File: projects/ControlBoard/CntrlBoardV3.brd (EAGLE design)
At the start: 76.2 x 76.2 mm, 122 parts, among them J1 HARWIN_06, J2 HARWIN_06, J3 M80-54006, J4 M80-54010, J5 M80-54008, J6 M80-54020, J7 M83-LMT1M2N27, J8 M80-5101005, J9 M50-3600542, M1 AON7522E, M2 SI4427BDY-T1-E3CT-ND, U1 MR25H40MDF, U10 LT6015, U11 LT6016, U12 TPS63001, U13 TPS63002, U14 MPU9250, U15 HMC5883L, U2 M24M02-DR, U3 SN74LVC1G125, U4 SN74LVC1G125, U6 MR25H40MDF, U7 AD7991-1, U8 LTC1380-GN, U9 LTC1380-GN

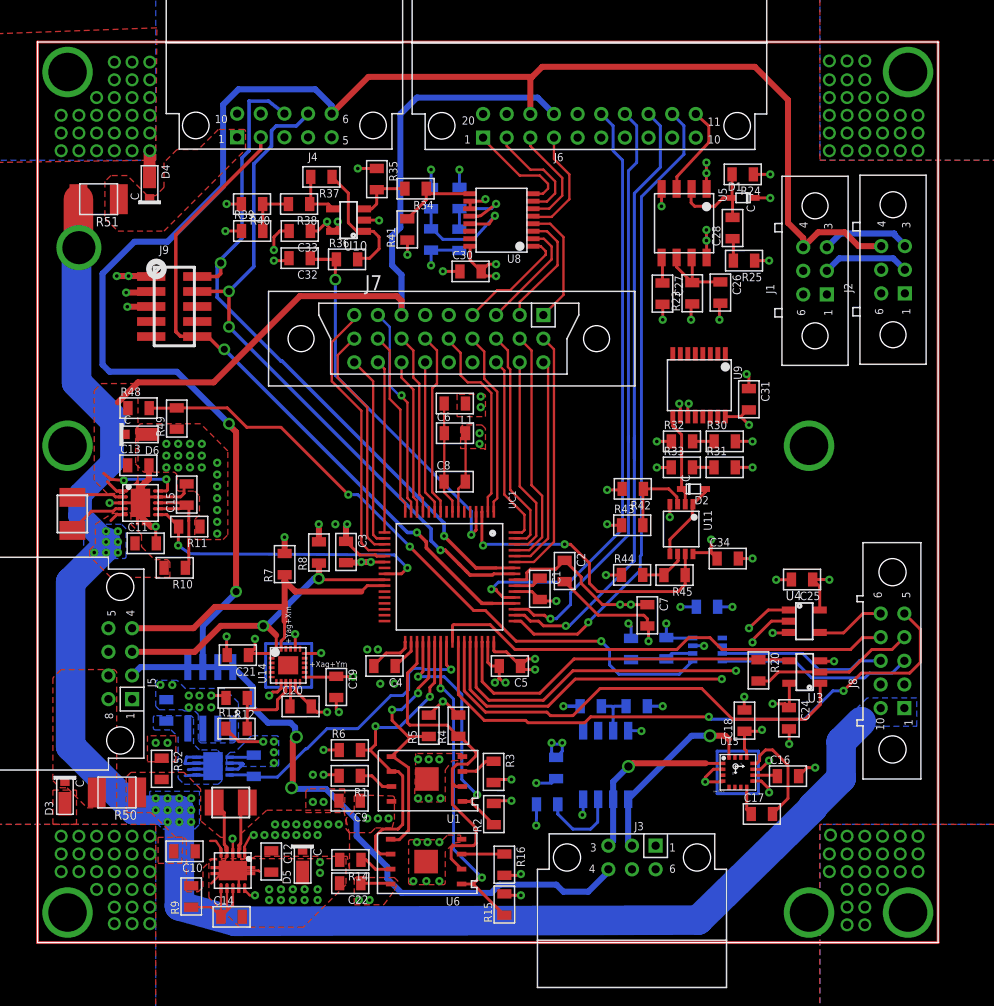
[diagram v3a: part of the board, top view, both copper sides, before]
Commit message: Completed first round of Control Board routing and silkscreen marker placement. Gonna sleep on it and see how I like it in the morning.
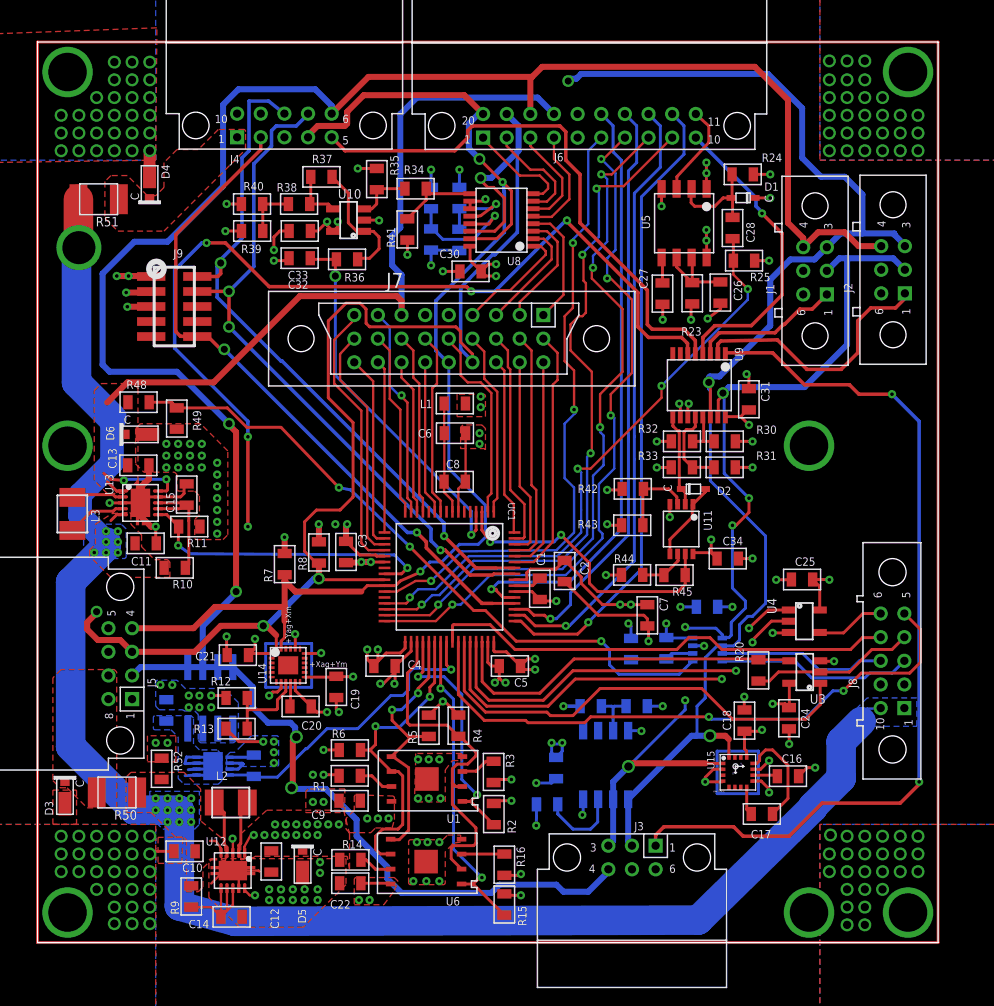
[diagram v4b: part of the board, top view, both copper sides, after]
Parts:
- moved R48 0.50 mm to (8.55, 45.7)
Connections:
- net PD_FLASH: now also U9.P$4; no longer U9.P$1
- net PD_XN: now also U9.P$2; no longer U9.P$3
- net PD_XP: now also U9.P$6; no longer U9.P$2
- net PD_YN: now also U9.P$3; no longer U9.P$4
- net PD_ZN: now also U9.P$5; no longer U9.P$6
- net PD_ZP: now also U9.P$1; no longer U9.P$5
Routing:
- net SDA: track 51.9 -> 331.7 mm, vias 3 -> 7
- net SCL: track 52.0 -> 264.9 mm, vias 1 -> 9
- net PD_XP: track 0.00 -> 99.4 mm, vias 0 -> 5
- net PD_ZP: track 0.00 -> 75.2 mm, vias 0 -> 2
- net ANT_DRV2: track 0.00 -> 60.0 mm, vias 0 -> 4
- net ANT_DRV1: track 0.00 -> 59.9 mm, vias 0 -> 4
- net ANT_DRV3: track 0.00 -> 59.7 mm, vias 0 -> 4
- net DET_RTN: track 0.00 -> 53.7 mm, vias 0 -> 3
- net !LED_CMD!: track 1.89 -> 51.8 mm, vias 0 -> 4
- net PD_ZN: track 0.00 -> 46.6 mm
- net PD_FLASH: track 0.00 -> 25.9 mm, vias 0 -> 1
- net PD_XN: track 0.00 -> 22.3 mm
- net N$32: track 15.2 -> 0.00 mm
- net N$31: track 15.2 -> 0.00 mm
- net N$30: track 14.2 -> 0.00 mm
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
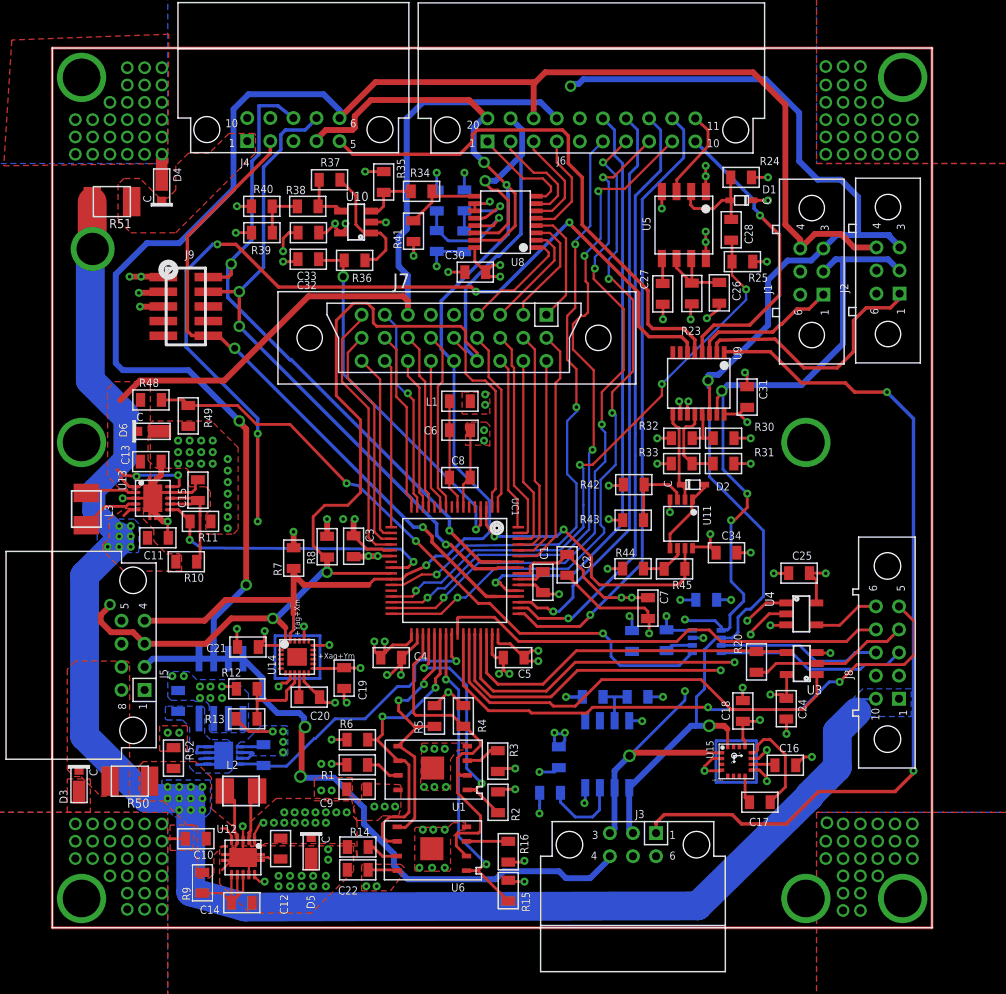
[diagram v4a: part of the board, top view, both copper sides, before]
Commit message: Added test vias and LEDs for testing and monitoring. Cleaned up asthetics and added documentation on silkscreen
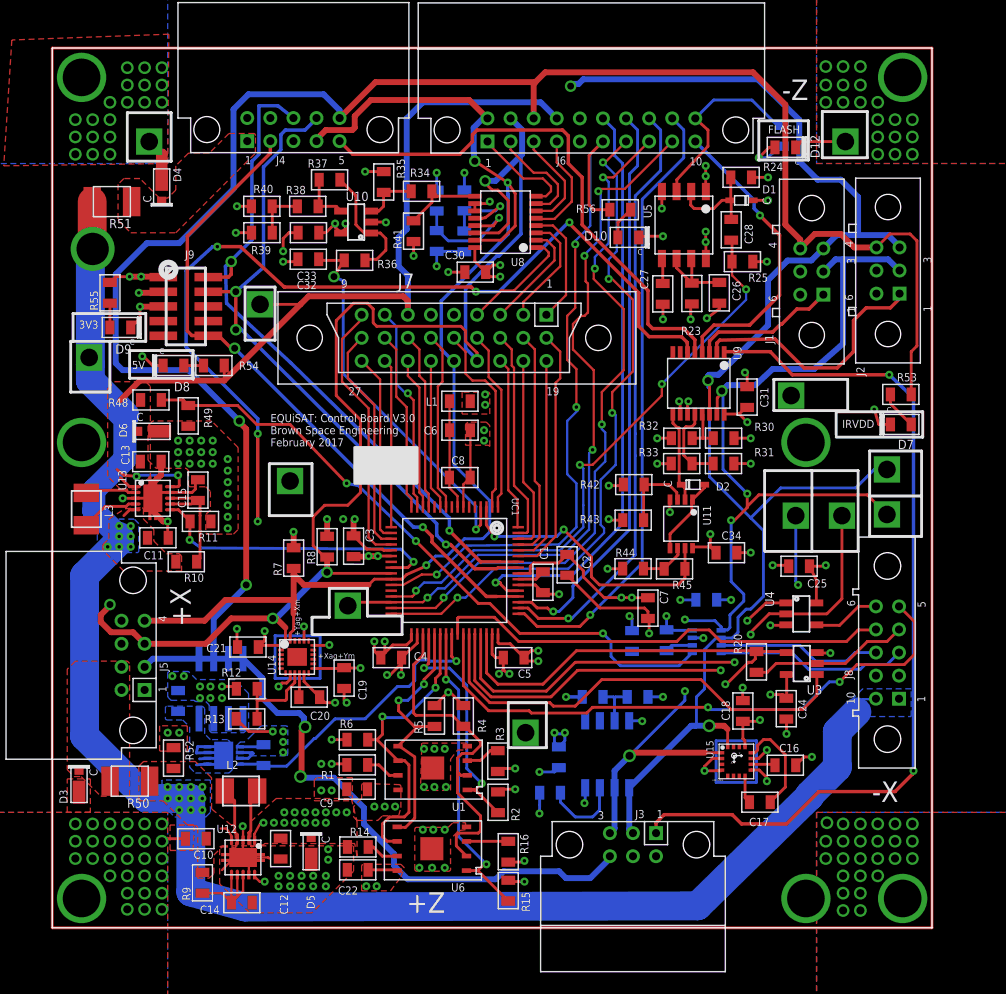
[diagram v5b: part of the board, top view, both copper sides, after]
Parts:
- added D10, D12, D7, D8, D9: LED0805, BrownSpaceEngineering:0805-D
- added R53, R55, R58: 330R, BrownSpaceEngineering:0805
- added R54, R56: 560R, BrownSpaceEngineering:0805
- added V1: RX_DATA, BrownSpaceEngineering:VIA-60MIL-SQ
- added V10, V11, V12, V9: GND, BrownSpaceEngineering:VIA-60MIL-SQ
- added V13: 3V3, BrownSpaceEngineering:VIA-60MIL-SQ
- added V14: 5V, BrownSpaceEngineering:VIA-60MIL-SQ
- added V2: TX_DATA, BrownSpaceEngineering:VIA-60MIL-SQ
- added V3: VIN, BrownSpaceEngineering:VIA-60MIL-SQ
- added V4: SDA, BrownSpaceEngineering:VIA-60MIL-SQ
- added V5: SCL, BrownSpaceEngineering:VIA-60MIL-SQ
- added V6: ANT_DRV1, BrownSpaceEngineering:VIA-60MIL-SQ
- moved C25 0.60 mm to (64.7, 31.3)
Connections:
- new net N$29: D7.A, R53.1
- new net N$30: D8.A, R54.1
- new net N$31: D9.A, R55.1
- new net N$40: D10.A, R56.1
- new net N$44: D12.A, R58.2
- net +3V3: now also R55.2, V13.P$1
- net +5V: now also R54.2, V14.P$1
- net ANT_DRV1: now also V6.P$1
- net DET_RTN: now also R56.2
- net GND: now also D10.C, D12.C, D7.C, D8.C, D9.C, V10.P$1, V11.P$1, V12.P$1, V9.P$1
- net IRVDD: now also R53.2
- net LED_SHDN: now also R58.1
- net RX_DATA: now also V1.P$1
- net SCL: now also V5.P$1
- net SDA: now also V4.P$1
- net TX_DATA: now also V2.P$1
- net VIN: now also V3.P$1
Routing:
- net RX_DATA: track 31.2 -> 52.6 mm, vias 0 -> 2
- net IRVDD: track 194.7 -> 212.4 mm
- net GND: track 144.8 -> 160.0 mm, vias 226 -> 211
- net SCL: track 264.9 -> 278.4 mm
- net SDA: track 331.7 -> 344.9 mm
- net TX_DATA: track 34.2 -> 46.8 mm
- net LED_SHDN: track 7.90 -> 17.0 mm
- net DET_RTN: track 53.7 -> 61.6 mm
- net +5V: track 70.4 -> 75.2 mm
- net N$44: track 0.00 -> 4.11 mm, vias 0 -> 1
- net ANT_DRV1: track 59.9 -> 63.7 mm
- net N$29: track 0.00 -> 3.35 mm
- net N$40: track 0.00 -> 2.86 mm
- net +3V3: track 123.0 -> 125.4 mm
- net N$31: track 0.00 -> 2.10 mm
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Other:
- board text added: "3V3"
- board text added: "5V"
- board text added: "EQUiSAT: Control Board V3.0 Brown Space Engineering February 2017"
- board text added: "FLASH"
- board text added: "IRVDD"

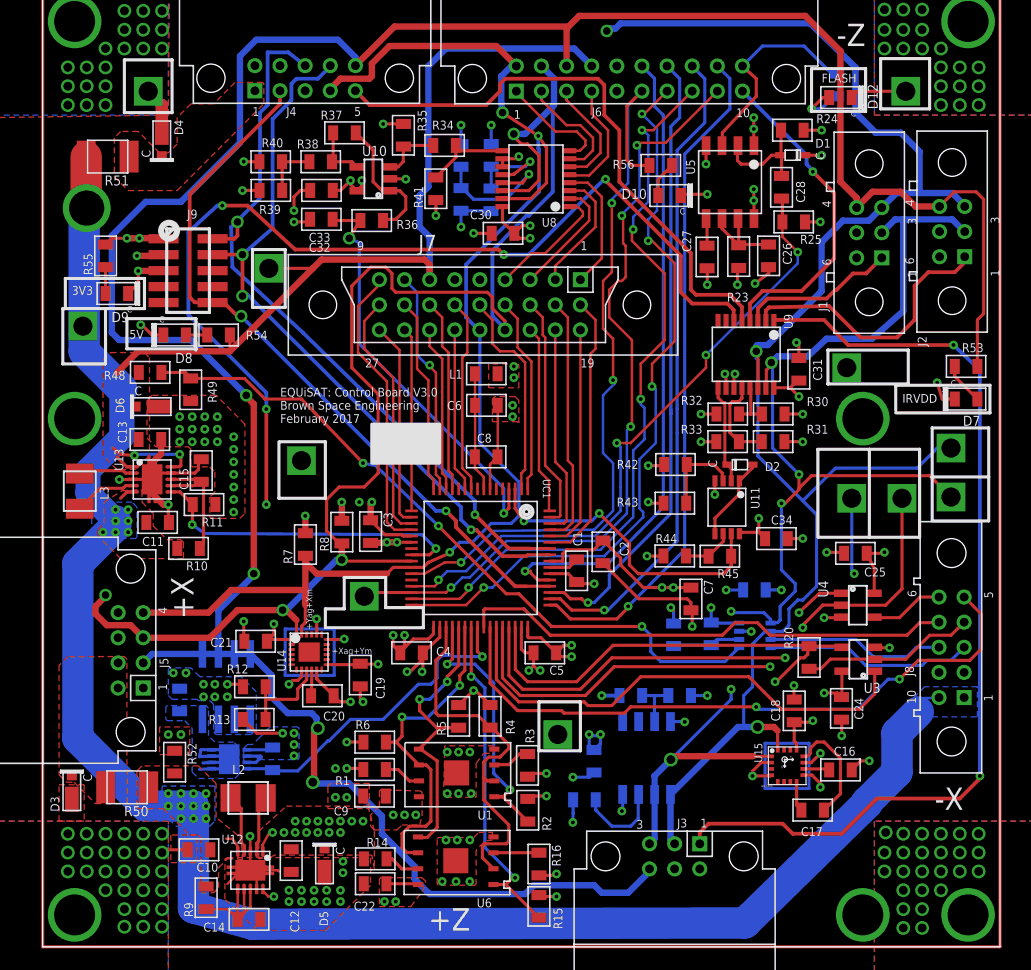
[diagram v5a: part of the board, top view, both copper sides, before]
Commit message: Cleaned up a few small things and corrected for errors discovered in DRC check.
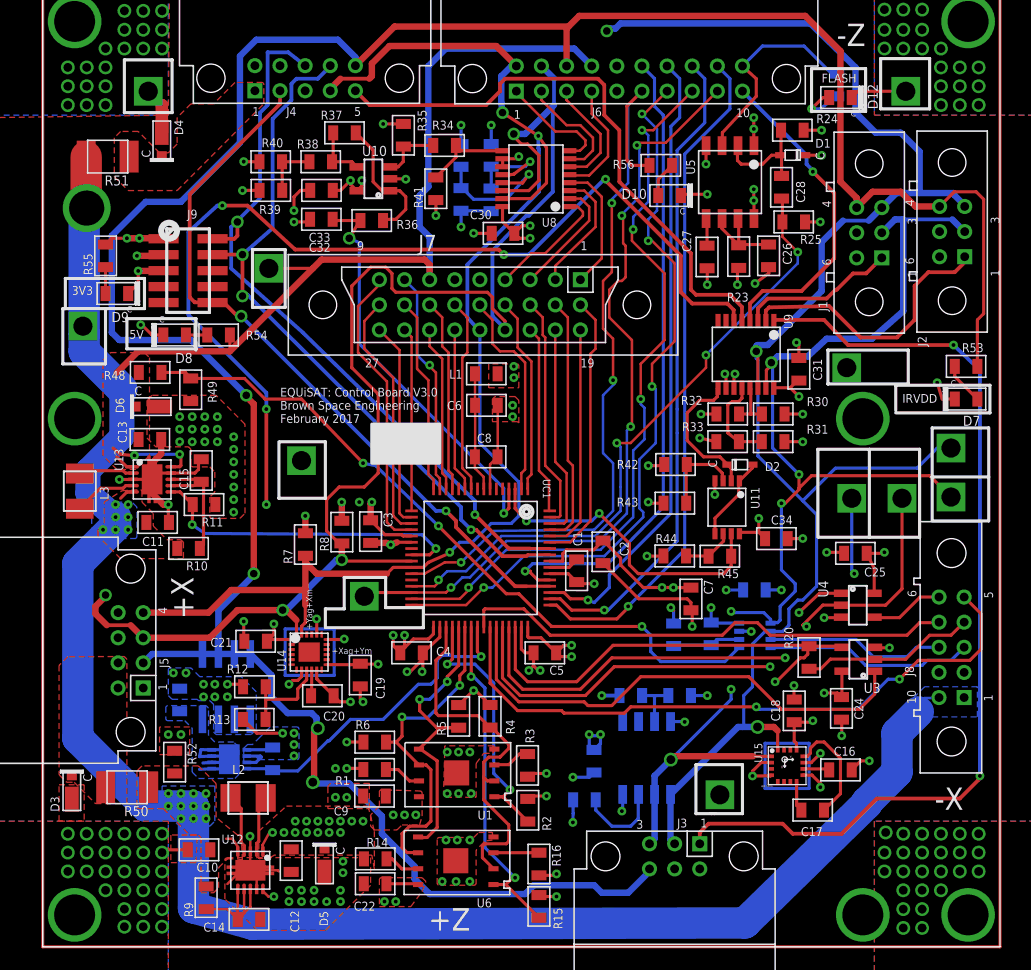
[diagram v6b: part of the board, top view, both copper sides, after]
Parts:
- moved V12 13.8 mm to (53.9, 12.1)
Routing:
- net PD_IN: track 7.92 -> 11.3 mm
- net GND: track 160.0 -> 160.1 mm, vias 211 -> 209
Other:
- board text removed: "Top layer is -Y side"

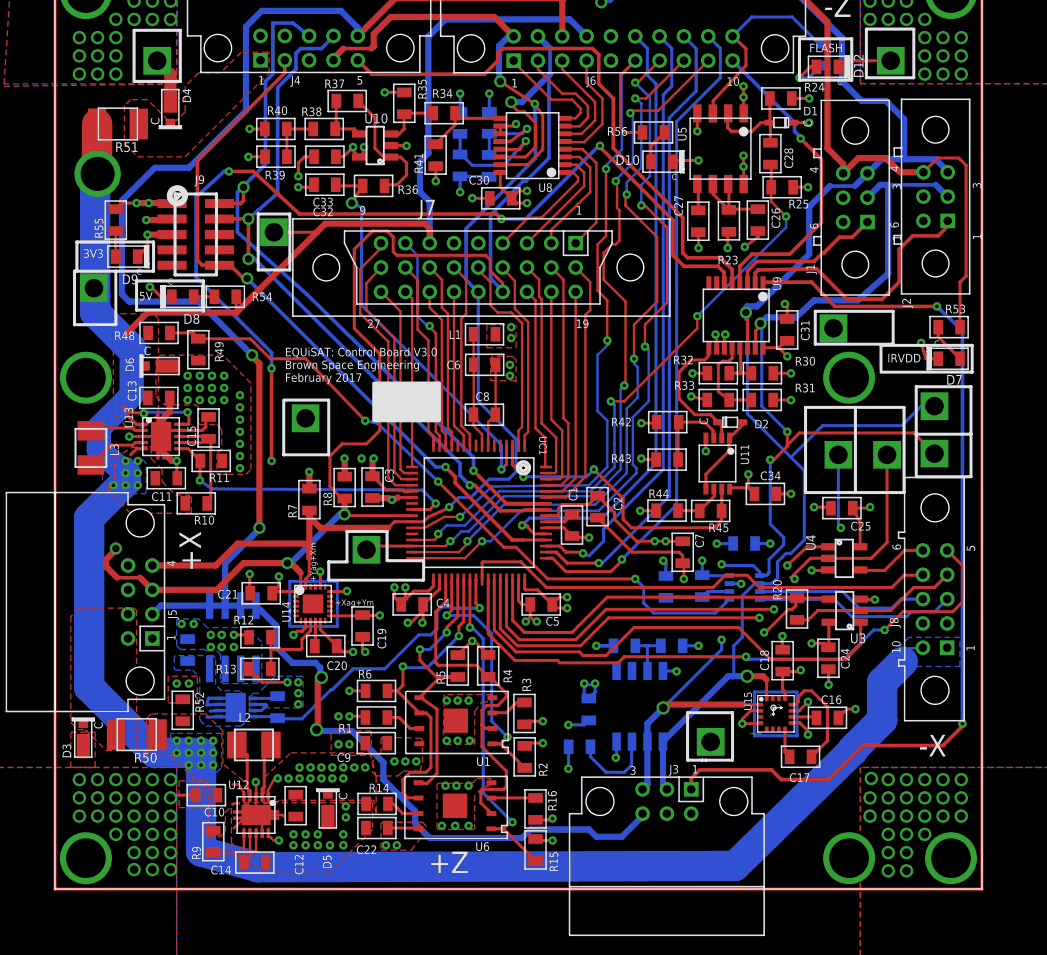
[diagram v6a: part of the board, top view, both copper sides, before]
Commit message: Fixed problem with processor pin mapping, rerouted accordingly. Final adjustments for production. Ready to order.
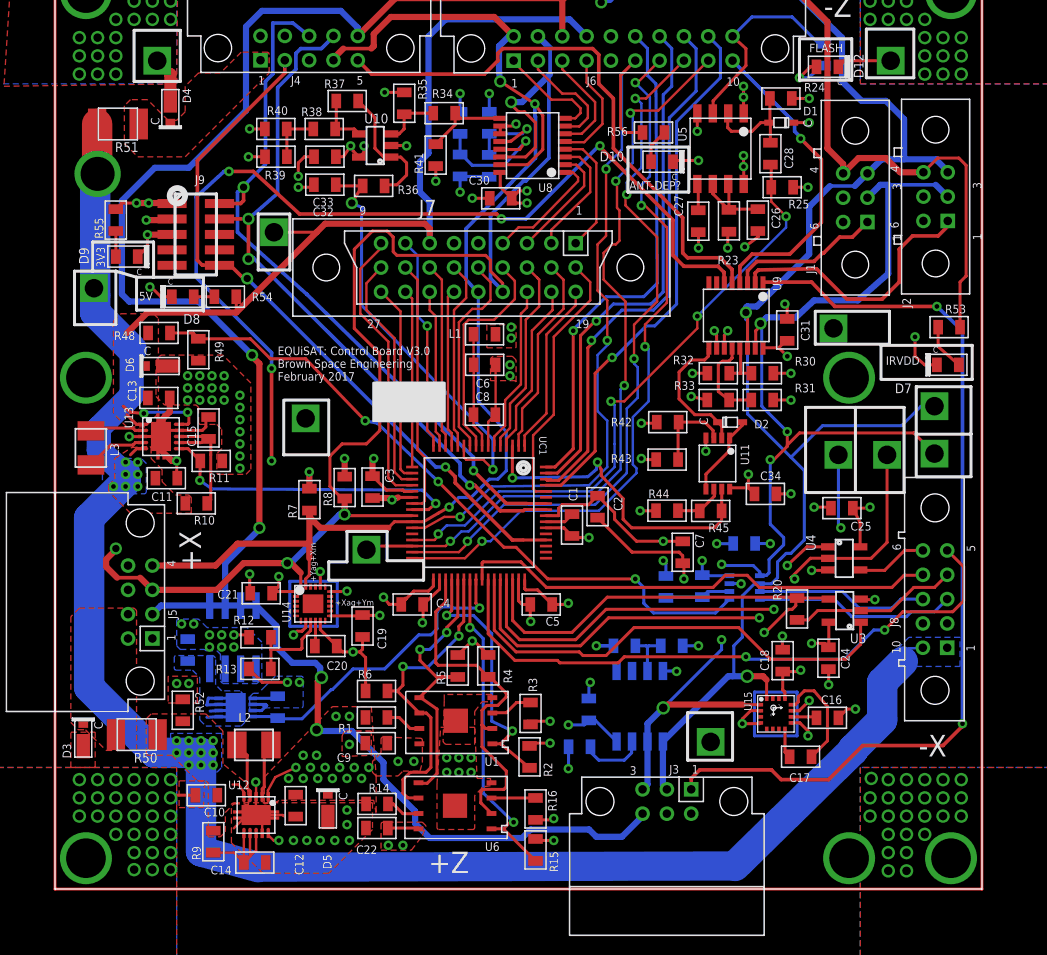
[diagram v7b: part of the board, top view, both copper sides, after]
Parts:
- moved D7 0.51 mm to (73.4, 43.1)
- moved R3 0.50 mm to (39.1, 14.4)
- moved R2 0.40 mm to (39.0, 10.9)
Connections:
- net L1_DISG: now also UC1.P$60; no longer UC1.P$59
- net L1_REF: now also J7.P$20, UC1.P$4; no longer J7.P$11, UC1.P$16
- net L1_RUN_CHG: now also UC1.P$2; no longer UC1.P$61
- net L2_DISG: now also UC1.P$1; no longer UC1.P$60
- net L2_REF: now also UC1.P$16; no longer UC1.P$15
- net L2_RUN_CHG: now also UC1.P$5; no longer UC1.P$63
- net LED1SNS: now also UC1.P$64; no longer UC1.P$53
- net LED2SNS: now also UC1.P$63; no longer UC1.P$51
- net LED3SNS: now also UC1.P$62; no longer UC1.P$50
- net LED4SNS: now also UC1.P$61; no longer UC1.P$49
- net LF1REF: now also UC1.P$15; no longer UC1.P$14
- net LF2REF: now also UC1.P$14; no longer UC1.P$13
- net LF3REF: now also UC1.P$12; no longer UC1.P$10
- net LF4REF: now also UC1.P$13; no longer UC1.P$11
- net LF_B1_OUTEN: now also UC1.P$9; no longer UC1.P$1
- net LF_B1_RUNCHG: now also UC1.P$6; no longer UC1.P$64
- net LF_B2_OUTEN: now also UC1.P$10; no longer UC1.P$2
- net LF_B2_RUNCHG: now also J7.P$11, UC1.P$23; no longer J7.P$20, UC1.P$62
- net TEMP_OUT: now also UC1.P$11; no longer UC1.P$4
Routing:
- net LED4SNS: track 53.9 -> 44.7 mm
- net LED1SNS: track 51.3 -> 42.3 mm
- net LED3SNS: track 51.9 -> 44.3 mm
- net LED2SNS: track 49.8 -> 43.0 mm
- net LF_B2_RUNCHG: track 17.0 -> 21.0 mm
- net L2_DISG: track 18.2 -> 14.4 mm
- net L1_RUN_CHG: track 20.0 -> 16.6 mm
- net LF_B1_OUTEN: track 15.6 -> 18.5 mm
- net L2_RUN_CHG: track 18.7 -> 16.6 mm
- net PD_OUT: track 25.3 -> 27.1 mm
- net N$18: track 6.92 -> 5.24 mm
- net L1_REF: track 15.6 -> 14.3 mm
- net LF_B1_RUNCHG: track 15.1 -> 13.8 mm
- net TEMP_OUT: track 33.3 -> 34.6 mm
- net SCL: track 278.2 -> 277.1 mm
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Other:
- board text added: "ANT-DEP?"
